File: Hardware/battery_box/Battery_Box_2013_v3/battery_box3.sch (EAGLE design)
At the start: 54 parts, among them IC1 AD826R, IC2 LM2574, IC3 PIC16F1824, IC4 LD117AS18TR, J1 CON_HEADER_PRG_PIC_ICSPA, Q1 IRFR5505PBFTO252, Q2 BSS123, X1 CON_MOLEX_39_29_1028

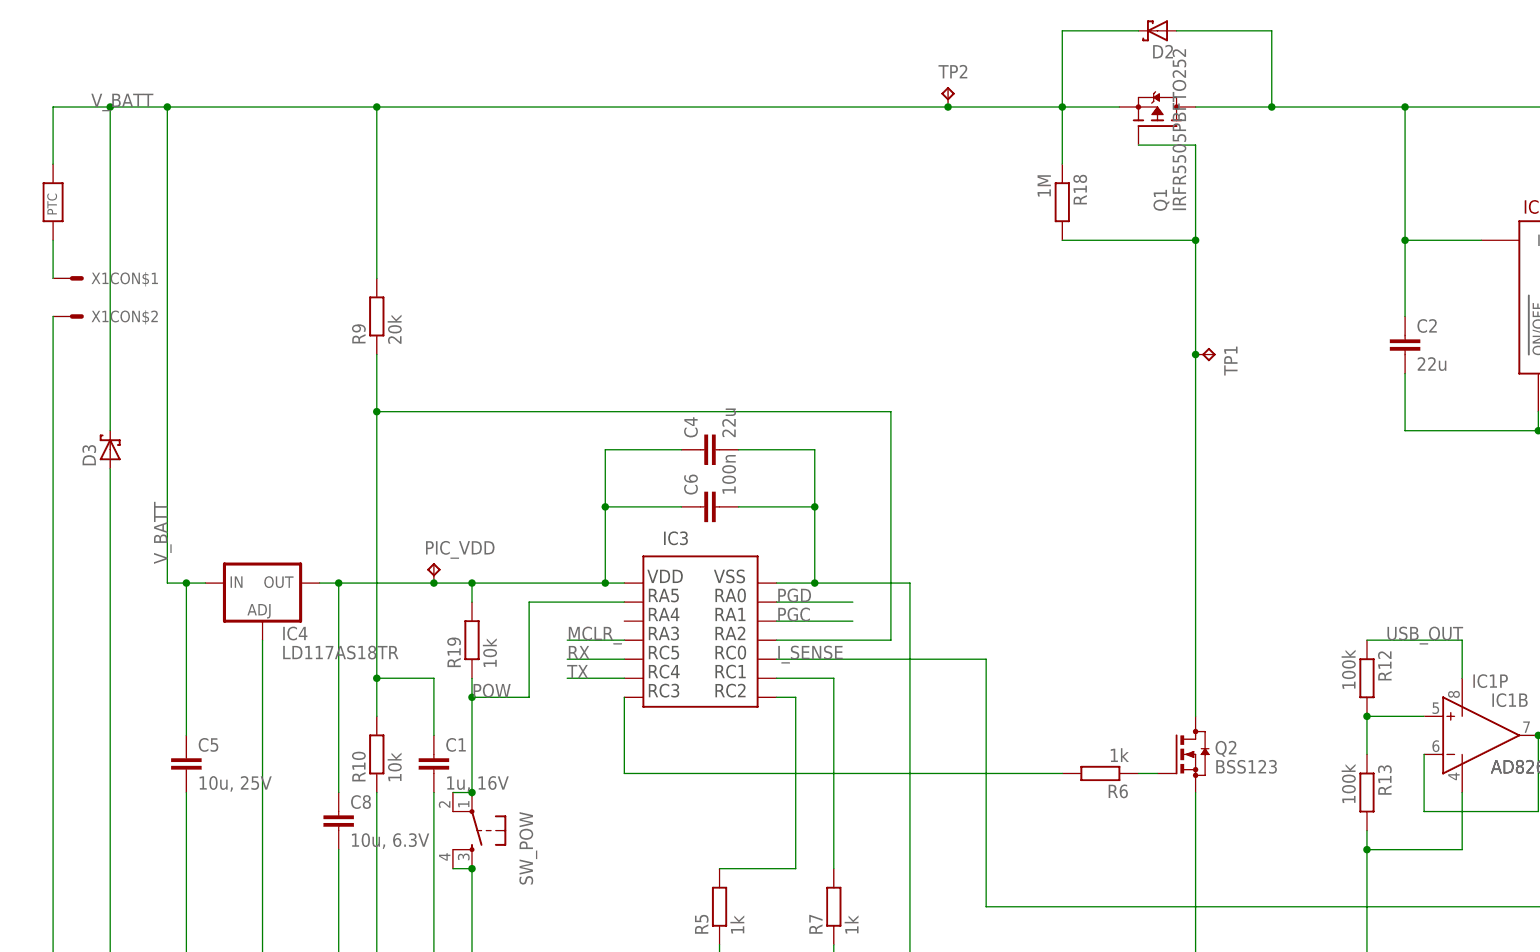
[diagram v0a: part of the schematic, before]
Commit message: Added Battery Box V3
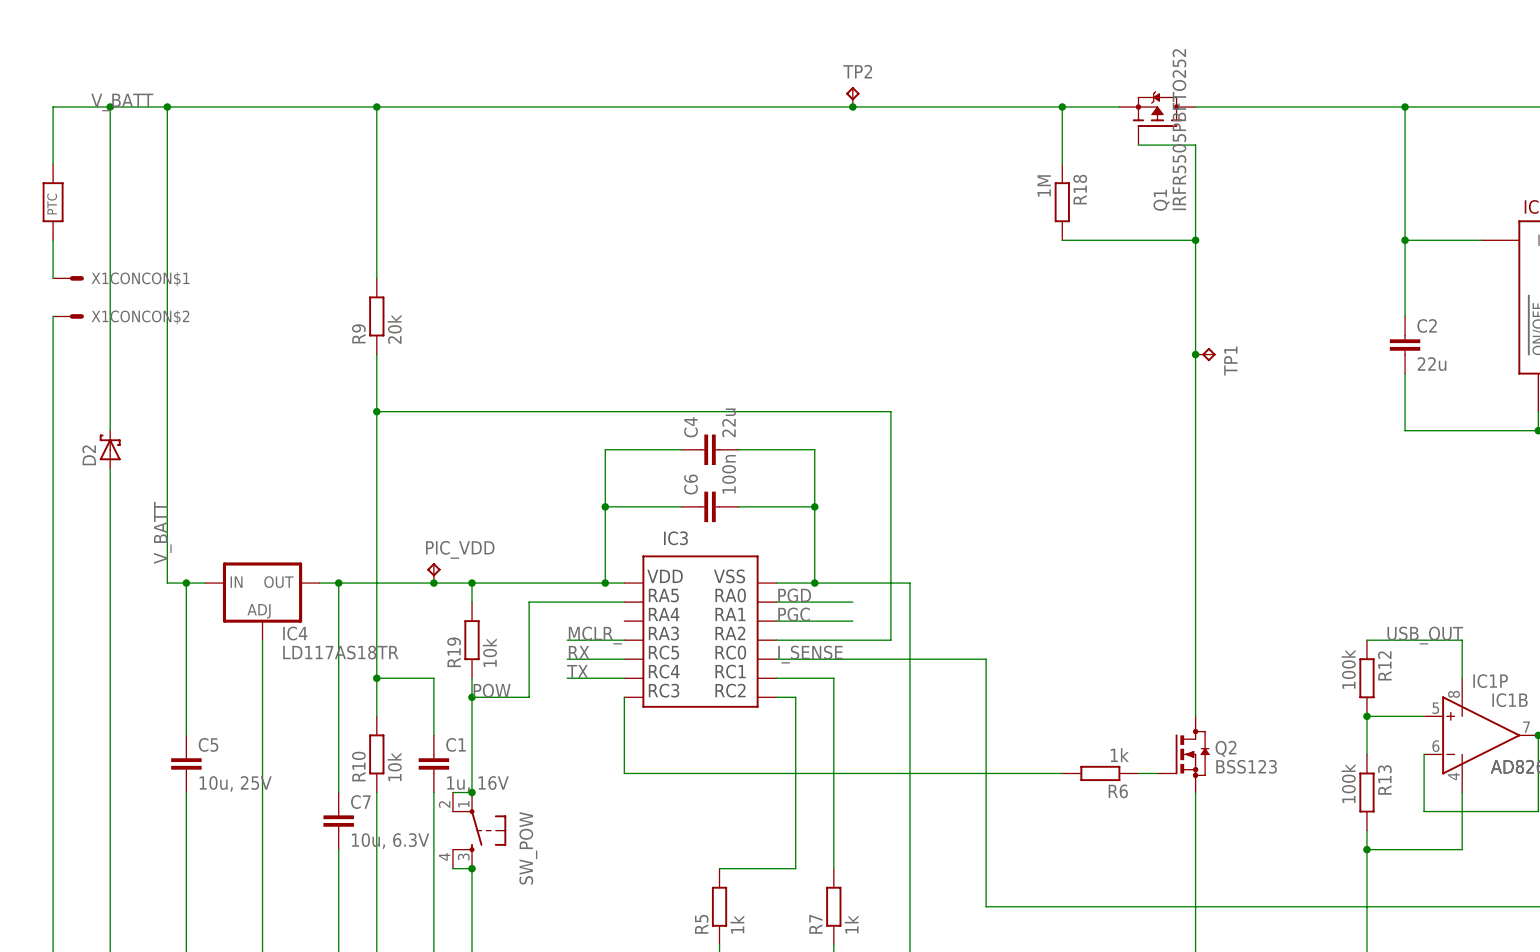
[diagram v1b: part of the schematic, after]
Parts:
- removed D3: (no value), diode:SCHOTTKY-DIODESMC
- removed U$1: EQUINOX_LOGO_SMALL, equinox:EQUINOX_LOGO_SMALL
- TP2: value TPTP14R -> TPTP20R; device testpad:TPTP14R -> testpad:TPTP20R
- renumbered C8 to C7, X1 to X1CON
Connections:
- net 12V_OUT: no longer D2.A
- net GND: now also D2.A; no longer D3.A
- net V_BATT: no longer D3.C
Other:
- moved on the sheet: D2, TP2
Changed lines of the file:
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@@
 <part name="U$7" library="equinox" deviceset="PCB_MOUNT_RICHO" device=""/>
 <part name="U$8" library="equinox" deviceset="PCB_MOUNT_RICHO" device=""/>
-<part name="X1" library="equinox" deviceset="CON_MOLEX_39_29_1028" device=""/>
+<part name="X1CON" library="equinox" deviceset="CON_MOLEX_39_29_1028" device=""/>
 <part name="R1" library="rcl" deviceset="R-EU_" device="R0805" value="75k"/>
 <part name="R2" library="rcl" deviceset="R-EU_" device="R0805" value="49.9k"/>
@@
 <part name="R19" library="rcl" deviceset="R-EU_" device="R0805" value="10k"/>
 <part name="DATA_OUT" library="con-lstb" deviceset="MA04-1" device=""/>
-<part name="U$1" library="equinox" deviceset="EQUINOX_LOGO_SMALL" device=""/>
 <part name="IC4" library="v-reg" deviceset="LD117A?*" device="S" technology="18TR"/>
 <part name="D2" library="diode" deviceset="SCHOTTKY-DIODE" device="SMC"/>
-<part name="D3" library="diode" deviceset="SCHOTTKY-DIODE" device="SMC"/>
-<part name="C8" library="rcl" deviceset="C-EU" device="C0805" value="10u, 6.3V"/>
+<part name="C7" library="rcl" deviceset="C-EU" device="C0805" value="10u, 6.3V"/>
 <part name="C5" library="rcl" deviceset="C-EU" device="C1210" value="10u, 25V"/>
 <part name="D1" library="diode" deviceset="SCHOTTKY-DIODE" device="SMD"/>
@@
 <part name="PIC_VDD" library="testpad" deviceset="TP" device="TP14R" value="TPTP14R"/>
 <part name="TP1" library="testpad" deviceset="TP" device="TP14R" value="TPTP14R"/>
-<part name="TP2" library="testpad" deviceset="TP" device="TP14R" value="TPTP14R"/>
+<part name="TP2" library="testpad" deviceset="TP" device="TP20R"/>
 </parts>
 <sheets>
@@
 <instance part="U$7" gate="G$1" x="220.98" y="10.16"/>
 <instance part="U$8" gate="G$1" x="233.68" y="10.16"/>
-<instance part="X1" gate="CON$1" x="27.94" y="160.02"/>
-<instance part="X1" gate="CON$2" x="27.94" y="154.94"/>
+<instance part="X1CON" gate="CON$1" x="27.94" y="160.02"/>
+<instance part="X1CON" gate="CON$2" x="27.94" y="154.94"/>
 <instance part="R1" gate="G$1" x="292.1" y="157.48" rot="R90"/>
 <instance part="R2" gate="G$1" x="292.1" y="144.78" rot="R90"/>
@@
 <instance part="R19" gate="G$1" x="81.28" y="111.76" rot="R90"/>
 <instance part="DATA_OUT" gate="1" x="68.58" y="22.86"/>
-<instance part="U$1" gate="G$1" x="314.96" y="12.7"/>
 <instance part="IC4" gate="G$1" x="53.34" y="119.38"/>
-<instance part="D2" gate="G$1" x="172.72" y="193.04" rot="R180"/>
-<instance part="D3" gate="G$1" x="33.02" y="137.16" rot="R90"/>
-<instance part="C8" gate="G$1" x="63.5" y="88.9"/>
+<instance part="D2" gate="G$1" x="33.02" y="137.16" rot="R90"/>
+<instance part="C7" gate="G$1" x="63.5" y="88.9"/>
 <instance part="C5" gate="G$1" x="43.18" y="96.52"/>
 <instance part="D1" gate="G$1" x="241.3" y="149.86" rot="R90"/>
@@
 <instance part="PIC_VDD" gate="G$1" x="76.2" y="121.92"/>
 <instance part="TP1" gate="G$1" x="180.34" y="149.86" rot="R270"/>
-<instance part="TP2" gate="G$1" x="144.78" y="185.42"/>
+<instance part="TP2" gate="G$1" x="132.08" y="185.42"/>
 </instances>
 <busses>
@@
 <wire x1="81.28" y1="119.38" x2="81.28" y2="116.84" width="0.1524" layer="91"/>
 <wire x1="109.22" y1="129.54" x2="99.06" y2="129.54" width="0.1524" layer="91"/>
-<pinref part="C8" gate="G$1" pin="1"/>
+<pinref part="C7" gate="G$1" pin="1"/>
 <wire x1="63.5" y1="91.44" x2="63.5" y2="119.38" width="0.1524" layer="91"/>
 <wire x1="63.5" y1="119.38" x2="60.96" y2="119.38" width="0.1524" layer="91"/>
@@
 <wire x1="200.66" y1="48.26" x2="345.44" y2="48.26" width="0.1524" layer="91"/>
 <wire x1="345.44" y1="48.26" x2="345.44" y2="114.3" width="0.1524" layer="91"/>
-<pinref part="X1" gate="CON$2" pin="S"/>
+<pinref part="X1CON" gate="CON$2" pin="S"/>
 <wire x1="25.4" y1="154.94" x2="25.4" y2="48.26" width="0.1524" layer="91"/>
 <pinref part="IC3" gate="G$1" pin="P$14"/>
@@
 <wire x1="53.34" y1="111.76" x2="53.34" y2="48.26" width="0.1524" layer="91"/>
 <wire x1="33.02" y1="134.62" x2="33.02" y2="48.26" width="0.1524" layer="91"/>
-<pinref part="D3" gate="G$1" pin="A"/>
-<pinref part="C8" gate="G$1" pin="2"/>
+<pinref part="D2" gate="G$1" pin="A"/>
+<pinref part="C7" gate="G$1" pin="2"/>
 <wire x1="63.5" y1="83.82" x2="63.5" y2="48.26" width="0.1524" layer="91"/>
 <pinref part="C5" gate="G$1" pin="2"/>
@@
 <junction x="40.64" y="182.88"/>
 <pinref part="U$2" gate="G$1" pin="P$2"/>
-<wire x1="160.02" y1="182.88" x2="144.78" y2="182.88" width="0.1524" layer="91"/>
-<wire x1="144.78" y1="182.88" x2="68.58" y2="182.88" width="0.1524" layer="91"/>
+<wire x1="160.02" y1="182.88" x2="132.08" y2="182.88" width="0.1524" layer="91"/>
+<wire x1="132.08" y1="182.88" x2="68.58" y2="182.88" width="0.1524" layer="91"/>
 <wire x1="68.58" y1="182.88" x2="40.64" y2="182.88" width="0.1524" layer="91"/>
 <wire x1="25.4" y1="175.26" x2="25.4" y2="182.88" width="0.1524" layer="91"/>
@@
 <junction x="160.02" y="182.88"/>
 <wire x1="33.02" y1="139.7" x2="33.02" y2="182.88" width="0.1524" layer="91"/>
-<wire x1="170.18" y1="193.04" x2="160.02" y2="193.04" width="0.1524" layer="91"/>
-<wire x1="160.02" y1="193.04" x2="160.02" y2="182.88" width="0.1524" layer="91"/>
 <label x="40.64" y="121.92" size="1.778" layer="95" rot="R90"/>
 <pinref part="IC4" gate="G$1" pin="IN"/>
 <wire x1="45.72" y1="119.38" x2="43.18" y2="119.38" width="0.1524" layer="91"/>
-<pinref part="D3" gate="G$1" pin="C"/>
 <pinref part="D2" gate="G$1" pin="C"/>
 <pinref part="C5" gate="G$1" pin="1"/>
 <wire x1="43.18" y1="119.38" x2="40.64" y2="119.38" width="0.1524" layer="91"/>
 <wire x1="43.18" y1="99.06" x2="43.18" y2="119.38" width="0.1524" layer="91"/>
-<pinref part="TP2" gate="G$1" pin="TP"/>
-<junction x="144.78" y="182.88"/>
 <junction x="43.18" y="119.38"/>
 <junction x="33.02" y="182.88"/>
+<pinref part="TP2" gate="G$1" pin="TP"/>
+<junction x="132.08" y="182.88"/>
 </segment>
 </net>
@@
 <segment>
 <pinref part="U$2" gate="G$1" pin="P$1"/>
-<pinref part="X1" gate="CON$1" pin="S"/>
+<pinref part="X1CON" gate="CON$1" pin="S"/>
 <wire x1="25.4" y1="165.1" x2="25.4" y2="160.02" width="0.1524" layer="91"/>
 </segment>
@@
 <junction x="340.36" y="182.88"/>
 <pinref part="IC2" gate="G$1" pin="IN"/>
-<wire x1="177.8" y1="182.88" x2="187.96" y2="182.88" width="0.1524" layer="91"/>
-<wire x1="187.96" y1="182.88" x2="205.74" y2="182.88" width="0.1524" layer="91"/>
+<wire x1="177.8" y1="182.88" x2="205.74" y2="182.88" width="0.1524" layer="91"/>
 <wire x1="205.74" y1="182.88" x2="279.4" y2="182.88" width="0.1524" layer="91"/>
 <wire x1="279.4" y1="182.88" x2="340.36" y2="182.88" width="0.1524" layer="91"/>
@@
 <wire x1="205.74" y1="154.94" x2="205.74" y2="165.1" width="0.1524" layer="91"/>
 <junction x="205.74" y="182.88"/>
-<wire x1="187.96" y1="182.88" x2="187.96" y2="193.04" width="0.1524" layer="91"/>
-<pinref part="D2" gate="G$1" pin="A"/>
-<wire x1="187.96" y1="193.04" x2="175.26" y2="193.04" width="0.1524" layer="91"/>
 <pinref part="12V_OUT" gate="G$1" pin="TP"/>
 <junction x="279.4" y="182.88"/>
-<junction x="187.96" y="182.88"/>
-</segment>
-</net>
+</segment>
+</net>
